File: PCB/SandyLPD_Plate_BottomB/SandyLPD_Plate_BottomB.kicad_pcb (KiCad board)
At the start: 2 copper layers, 131 x 83 mm, 141 parts, among them J1 Conn_02x02_Odd_Even, J2 Conn_01x03, J4 Conn_01x10_Pin, J5 USB_C_Receptacle_USB2.0, J6 USB_C_Receptacle_USB2.0, SW1 BOOT_ALT, SW2 RESET_ALT, SW3 SW_DIP_x04, U1 NCP1117-3.3_SOT223, U3 RP2040, U4 W25Q128JVPIQ, Y1 12MHz

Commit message: ボトムプレートの左右幅調整 #18
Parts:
- REF**: footprint locallib:SandyLP-Duo_outline_BottomB -> locallib:SandyLP-Duo_outline_BottomB_narrow_edge
- moved C11 122.1 mm to (210.1, 177.4)
- moved C2 122.1 mm to (185.0, 158.3)
- moved C3 122.1 mm to (206.8, 172.3)
- moved C4 122.1 mm to (203.0, 186.8)
- moved C5 122.1 mm to (205.8, 172.3)
- moved C6 122.1 mm to (204.0, 186.8)
- moved C7 122.1 mm to (199.1, 176.8)
- moved C8 122.1 mm to (198.1, 181.9)
- moved D25 122.1 mm to (144.3, 221.1)
- moved D26 122.1 mm to (163.3, 221.1)
- moved D27 122.1 mm to (184.8, 221.1)
- moved H_btm_1 122.1 mm to (136.0, 192.5)
- moved H_mid_1 122.1 mm to (102.6, 153.2)
- moved H_mid_10 122.1 mm to (196.7, 173.5)
- moved H_mid_17 122.1 mm to (220.5, 208.0)
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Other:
- board size 131 x 83 mm -> 124.4 x 83 mm
- board text added: "#SandyLP_Duo DN0010"
- board text removed: "#SandyLP_kbd DN0010, Base by @jpskenn github.com/jpskenn/SandyLP"

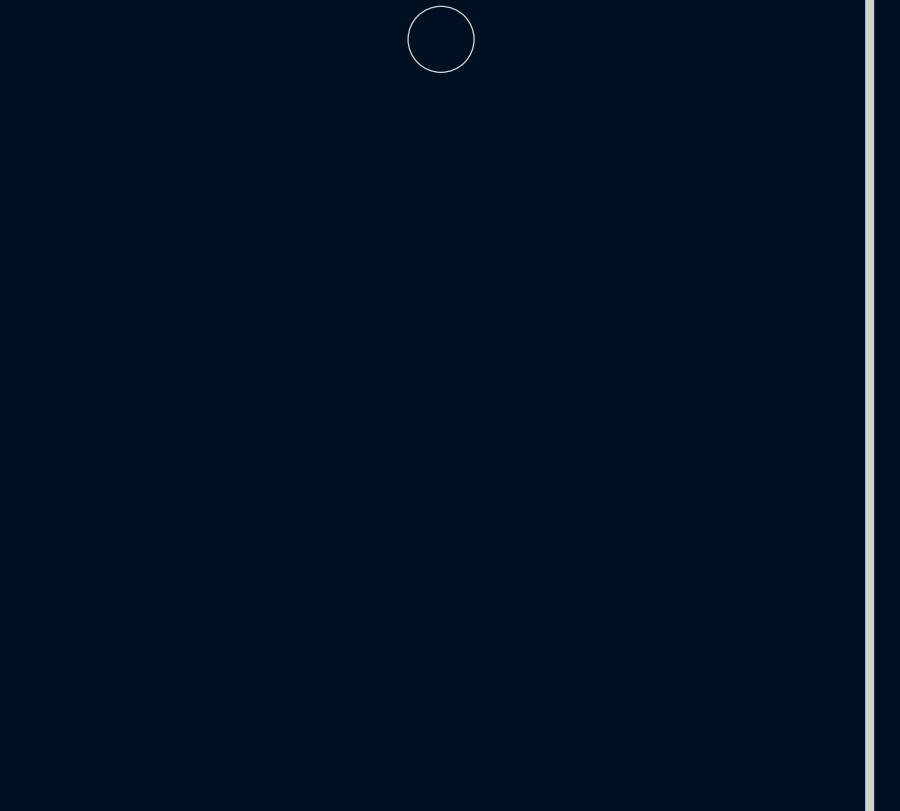
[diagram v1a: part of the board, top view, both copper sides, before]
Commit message: リセットスイッチ穴追加。USBまわり少し拡大
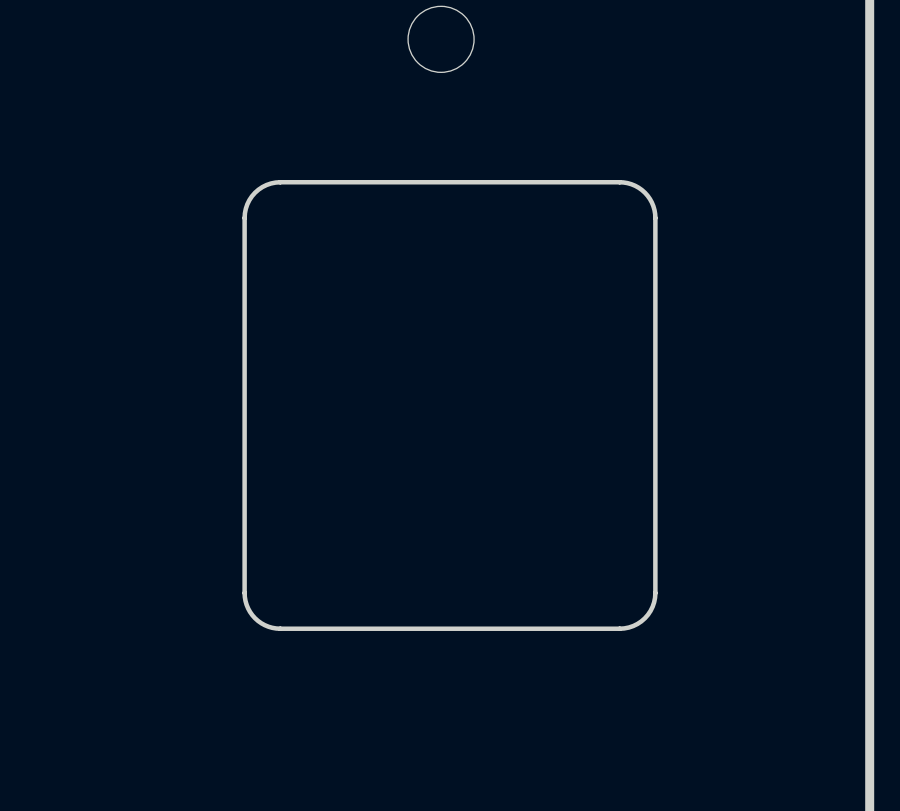
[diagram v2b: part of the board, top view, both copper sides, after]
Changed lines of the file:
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@@
 		(layer "Eco2.User")
 	)
+	(gr_line
+		(start 133.57259 80.581933)
+		(end 133.57259 93.083506)
+		(locked yes)
+		(stroke
+			(width 0.15)
+			(type default)
+		)
+		(layer "Edge.Cuts")
+	)
+	(gr_line
+		(start 134.763216 79.391307)
+		(end 146.074163 79.391307)
+		(locked yes)
+		(stroke
+			(width 0.15)
+			(type default)
+		)
+		(layer "Edge.Cuts")
+	)
+	(gr_arc
+		(start 146.074163 79.391307)
+		(mid 146.916066 79.74003)
+		(end 147.264789 80.581933)
+		(locked yes)
+		(stroke
+			(width 0.15)
+			(type default)
+		)
+		(layer "Edge.Cuts")
+	)
+	(gr_arc
+		(start 147.264789 93.083506)
+		(mid 146.916032 93.925375)
+		(end 146.074163 94.274132)
+		(locked yes)
+		(stroke
+			(width 0.15)
+			(type default)
+		)
+		(layer "Edge.Cuts")
+	)
+	(gr_arc
+		(start 133.57259 80.581933)
+		(mid 133.921333 79.74005)
+		(end 134.763216 79.391307)
+		(locked yes)
+		(stroke
+			(width 0.15)
+			(type default)
+		)
+		(layer "Edge.Cuts")
+	)
+	(gr_line
+		(start 147.264789 93.083506)
+		(end 147.264789 80.581933)
+		(locked yes)
+		(stroke
+			(width 0.15)
+			(type default)
+		)
+		(layer "Edge.Cuts")
+	)
+	(gr_arc
+		(start 134.763216 94.274132)
+		(mid 133.921299 93.925423)
+		(end 133.57259 93.083506)
+		(locked yes)
+		(stroke
+			(width 0.15)
+			(type default)
+		)
+		(layer "Edge.Cuts")
+	)
+	(gr_line
+		(start 146.074163 94.274132)
+		(end 134.763216 94.274132)
+		(locked yes)
+		(stroke
+			(width 0.15)
+			(type default)
+		)
+		(layer "Edge.Cuts")
+	)
 	(gr_text "#SandyLP_Duo DN0010"
 		(at 90.114741 112.728475 0)
@@
 		(members "3084c386-9d6e-4b65-ab72-6f6d9e9c5085" "f1620524-97c5-4beb-b292-3f5af92c31ac")
 	)
+	(group ""
+		(locked yes)
+		(members "016760aa-557b-449f-9ca5-2ed6fd610973" "2f9d6a8a-c6cb-4ee6-9f6a-2827fb0c839e"
+			"463454ad-c4a2-460b-a728-83968a9e9837" "4937af41-0b68-4674-af9c-224d071026fc"
+			"539e74ff-96b7-48bb-acc4-4c7b0d36a488" "6b6362f2-3d0a-4565-adac-38f261fa4f51"
+			"732edb18-2808-47d4-b4bf-c489b046b1aa" "9d0a6008-6d3c-46be-b368-85e8df2068e4"
+		)
+	)
 )

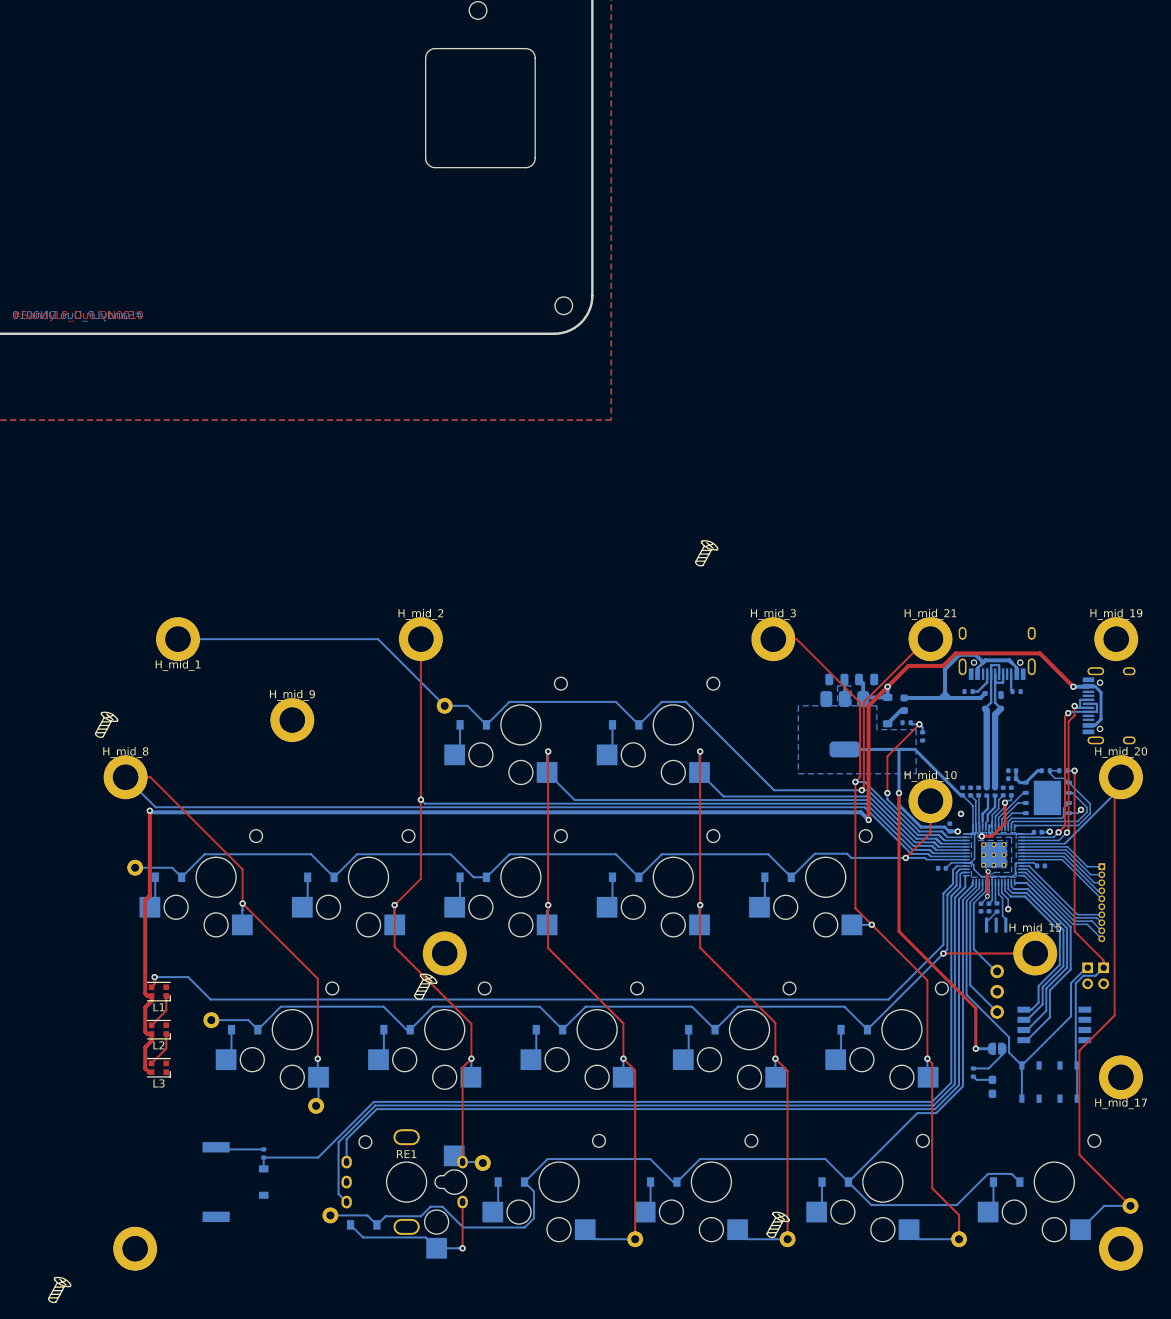
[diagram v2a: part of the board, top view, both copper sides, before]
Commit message: 電源LED位置調整。ボトムA,Bのリセット穴サイズ変更。Fusion用STEP出力。
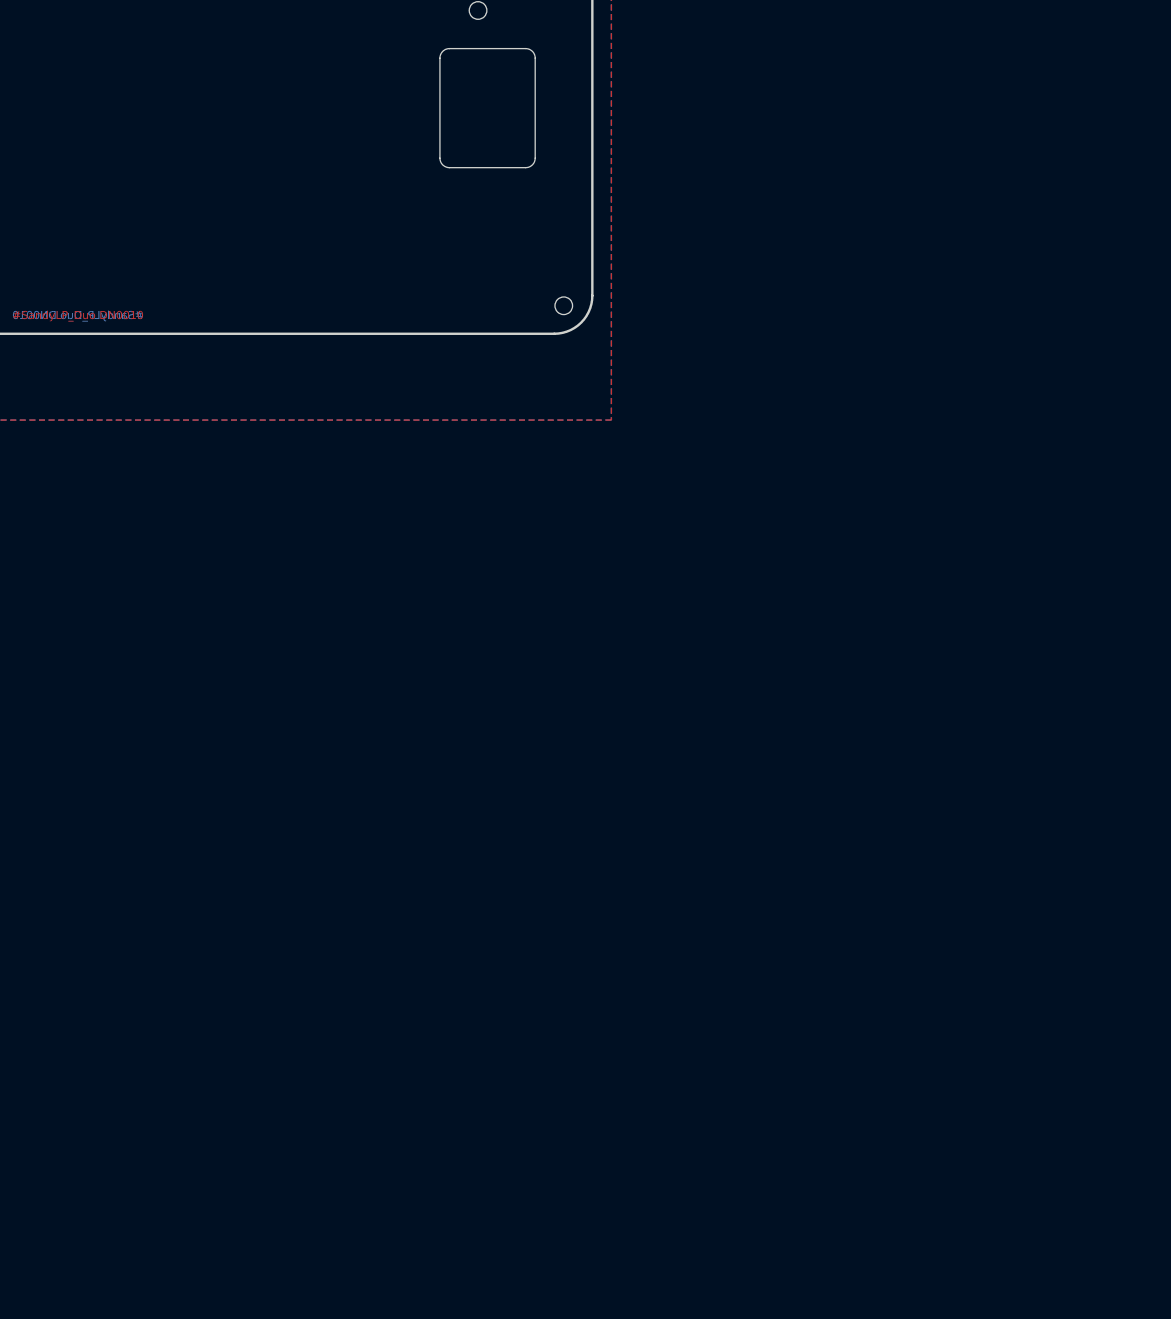
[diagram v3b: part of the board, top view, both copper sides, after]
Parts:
- removed C1, C2: 10u, Capacitor_SMD:C_0805_2012Metric
- removed C10, C11, C12, C3, C4, C5, C6, C7, C8, C9: 100n, Capacitor_SMD:C_0402_1005Metric
- removed C13, C14, C15: 2.2uF, Capacitor_SMD:C_0402_1005Metric
- removed D1, D15, D16, D17, D18, D19, D2, D25, D26, D27, D28, D33, D35, D5, D6, D7, D8, D9: D, locallib:D_SOD-123_Emphasized_Direction_Line_Reference_on_bottom
- removed D36: PRTR5V0U2X, Package_TO_SOT_SMD:SOT-143
- removed F1: Fuse, Fuse:Fuse_0603_1608Metric
- removed the H_btm_1 at (136.0, 192.5)
- removed the H_btm_3 at (97.3, 229.4)
- removed the H_btm_4 at (220.5, 229.4)
- removed the H_mid_1 at (102.6, 153.2)
- removed H_mid_10, H_mid_17, H_mid_2, H_mid_3, H_mid_8, H_mid_9: MountingHole, locallib:MountingHole_M2_Through-hole_tap_THC-0.8-x-2
- removed the H_mid_15 at (209.8, 192.5)
- removed the H_mid_19 at (219.9, 153.2)
- removed the H_mid_20 at (220.5, 170.5)
- removed the H_mid_21 at (196.7, 153.2)
- removed J1: Conn_02x02_Odd_Even, locallib:PinHeader_2x02_P2.00mm_Vertical_2pair
- removed J2: Conn_01x03, locallib:PinHeader_1x03_P2.54mm_Vertical_All_circle
- removed J4: Conn_01x10_Pin, Connector_PinHeader_1.00mm:PinHeader_1x10_P1.00mm_Vertical
- removed J5, J6: USB_C_Receptacle_USB2.0, locallib:USB_C_Receptacle_HRO_TYPE-C-31-M-12
- removed JP1: SolderJumper_2_Open, Jumper:SolderJumper-2_P1.3mm_Open_RoundedPad1.0x1.5mm
- removed L1, L2, L3: WS2812B-2020, LED_SMD:LED_WS2812B-2020_PLCC4_2.0x2.0mm
- removed LS1: Speaker, Buzzer_Beeper:Buzzer_Murata_PKMCS0909E
- removed R1, R5, R6, R9: 1k, Resistor_SMD:R_0402_1005Metric
- removed R10, R11: 5.1k, Resistor_SMD:R_0402_1005Metric
- removed R12: 5.6k, Resistor_SMD:R_0402_1005Metric
- removed R2, R3: 27, Resistor_SMD:R_0402_1005Metric
- removed R4, R8: 10k, Resistor_SMD:R_0402_1005Metric
- removed the REF** at (177.5, 229.0)
- removed the REF** at (97.5, 172.1)
- removed the REF** at (180.6, 144.3)
- removed the REF** at (104.1, 147.7)
- removed the REF** at (194.9, 178.7)
- removed the REF** at (130.6, 148.4)
- removed the REF** at (103.8, 145.5)
- removed the REF** at (194.3, 177.0)
- removed the REF** at (86.5, 235.7)
- removed the REF** at (93.7, 166.6)
- removed the REF** at (180.2, 142.4)
- removed the REF** at (87.7, 237.1)
- removed the REF** at (191.2, 144.1)
- removed the REF** at (97.0, 170.5)
- removed the REF** at (184.2, 142.5)
- removed the REF** at (190.7, 142.5)
- removed the REF** at (184.8, 144.0)
- removed the REF** at (114.5, 166.8)
- removed the REF** at (176.4, 229.1)
- removed the REF** at (114.9, 168.4)
- removed the REF** at (93.6, 166.5)
- removed the REF** at (168.6, 145.1)
- removed the REF** at (133.5, 199.2)
- removed the REF** at (130.2, 146.8)
- removed the REF** at (132.9, 199.4)
- removed SD1: Schottky diode, Diode_SMD:D_SOD-123
- removed STLED1: LED_GREEN, LED_SMD:LED_0603_1608Metric_Pad1.05x0.95mm_HandSolder
- removed SW1: BOOT_ALT, Button_Switch_SMD:SW_SPST_PTS810
- removed SW2: RESET_ALT, Button_Switch_SMD:SW_SPST_PTS810
- removed SW3: SW_DIP_x04, Button_Switch_SMD:SW_DIP_SPSTx04_Slide_Copal_CHS-04B_W7.62mm_P1.27mm
- removed SW_1: W, locallib:Kailh_socket_ChocV2
- removed SW_15: Z, locallib:Kailh_socket_ChocV2
- removed SW_16: X, locallib:Kailh_socket_ChocV2
- removed SW_17: C, locallib:Kailh_socket_ChocV2
- removed SW_18: V, locallib:Kailh_socket_ChocV2
- removed SW_19: B, locallib:Kailh_socket_ChocV2
- removed SW_2: E, locallib:Kailh_socket_ChocV2
- removed SW_25: L_RE, locallib:ChocV2_AND_RotaryEncoder_Alps_EC11K-Switch_Vertical_H20mm_NPTH_MP_minimal
- removed SW_27: LALT, locallib:Kailh_socket_ChocV2
- removed SW_28: LSPC, locallib:Kailh_socket_ChocV2
- removed SW_29: L_CNT, locallib:Kailh_socket_ChocV2
- removed SW_5: LCTL, locallib:Kailh_socket_ChocV2
- removed SW_6: A, locallib:Kailh_socket_ChocV2
- removed SW_7: S, locallib:Kailh_socket_ChocV2
- removed SW_8: D, locallib:Kailh_socket_ChocV2
- removed SW_9: F, locallib:Kailh_socket_ChocV2
- removed SW_LWIN1: LWIN, locallib:Kailh_socket_ChocV2
- removed T_L_C0, T_L_C1, T_L_C2, T_L_C3, T_L_C4, T_L_C5, T_L_R0, T_L_R1, T_L_R2, T_L_R3: Conn_01x01, locallib:TestPoint_THTPad_D2.0mm_Drill1.0mm
- removed U1: NCP1117-3.3_SOT223, Package_TO_SOT_SMD:SOT-223-3_TabPin2
- removed U3: RP2040, locallib:RP2040-QFN-56
- removed U4: W25Q128JVPIQ, Package_SON:WSON-8-1EP_6x5mm_P1.27mm_EP3.4x4.3mm
- removed Y1: 12MHz, Crystal:Resonator_SMD_Murata_CSTxExxV-3Pin_3.0x1.1mm
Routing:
- net (no net): track 905.9 -> 0.00 mm, vias 13 -> 0
- net +5V: track 186.2 -> 0.00 mm, vias 4 -> 0
- net L_row3: track 148.8 -> 0.00 mm
- net L_col2: track 137.1 -> 0.00 mm, vias 3 -> 0
- net +3V3: track 127.3 -> 0.00 mm, vias 3 -> 0
- net L_Audio: track 118.6 -> 0.00 mm
- net L_col3: track 118.3 -> 0.00 mm, vias 3 -> 0
- net L_LED: track 115.7 -> 0.00 mm, vias 1 -> 0
- net L_RE_B: track 114.6 -> 0.00 mm
- net L_RE_A: track 108.3 -> 0.00 mm
- net L_RESET: track 46.3 -> 0.00 mm
- net L_USB_BOOT: track 45.8 -> 0.00 mm, vias 1 -> 0
- net VBUS: track 28.8 -> 0.00 mm
- net L_RX: track 27.2 -> 0.00 mm, vias 2 -> 0
- net L_VBUS_detection: track 26.8 -> 0.00 mm, vias 2 -> 0
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- removed copper zone on B.Cu, net (none)
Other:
- board text removed: "Through-hole tap head diameter"
- board text removed: "参考 Base基板 左手"

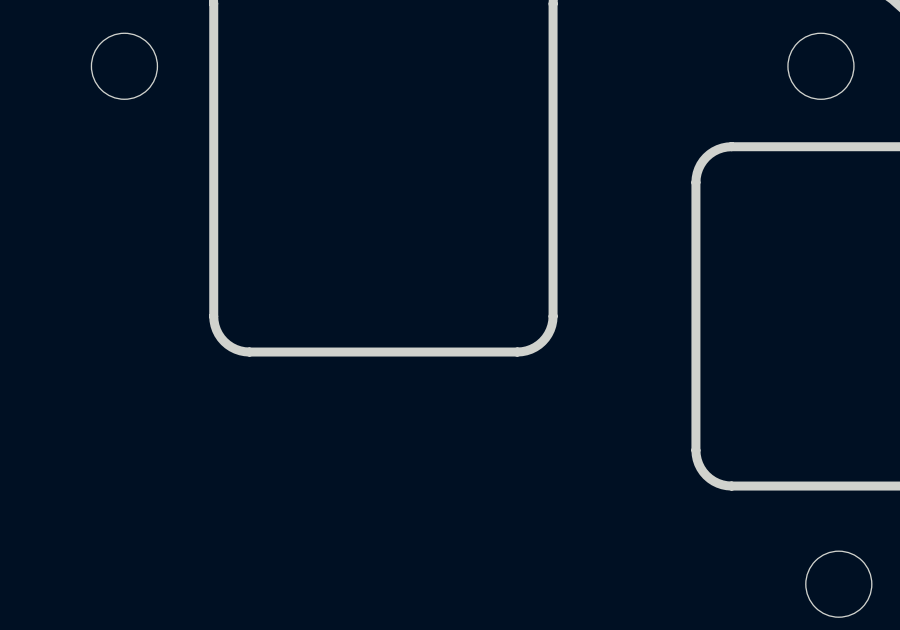
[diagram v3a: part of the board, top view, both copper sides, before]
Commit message: 間違い防止のシルク #30
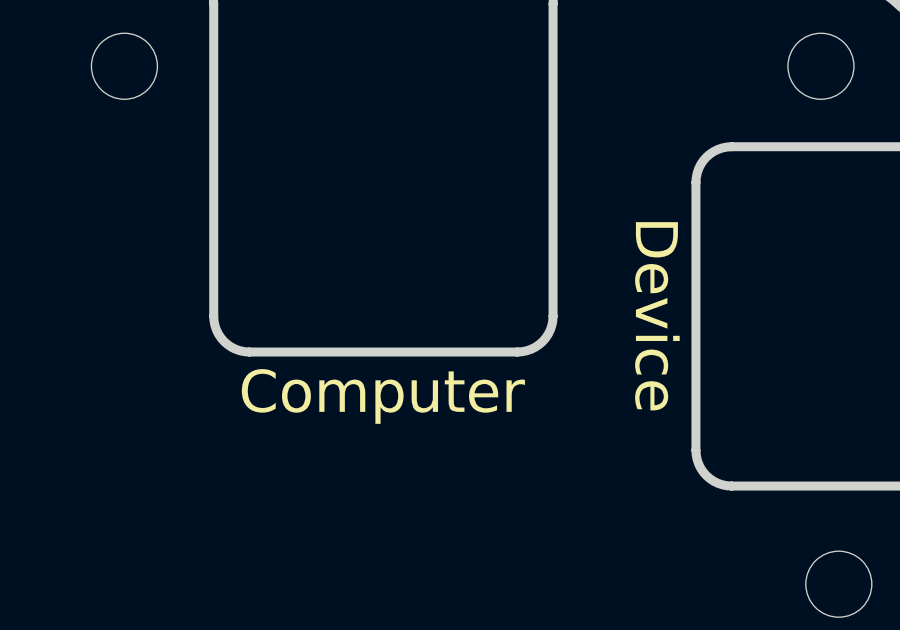
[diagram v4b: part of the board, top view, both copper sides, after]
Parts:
- removed the REF** at (99.0, 27.3)
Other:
- board text added: "Computer"
- board text added: "Device"
- board text removed: "Back Side"
- board text removed: "Fairness, Justice, Rightness"
- board text removed: "Screw for Top plate"

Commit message: WIP　ボトムプレートへの記載を試し中
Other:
- board text added: "⌨️"
